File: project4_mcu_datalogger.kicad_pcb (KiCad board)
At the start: 2 copper layers, 49.6 x 30.5 mm, 30 parts, among them J1 Conn_01x09_Pin, J2 Conn_01x04_Pin, J3 Conn_01x04_Pin, J4 Conn_02x03_Odd_Even, U1 24LC1025, U2 DS1337S_T_R, U3 24LC1025, U4 ATMEGA328P-AU, Y1 32.768 KHz, Y2 16 MHz

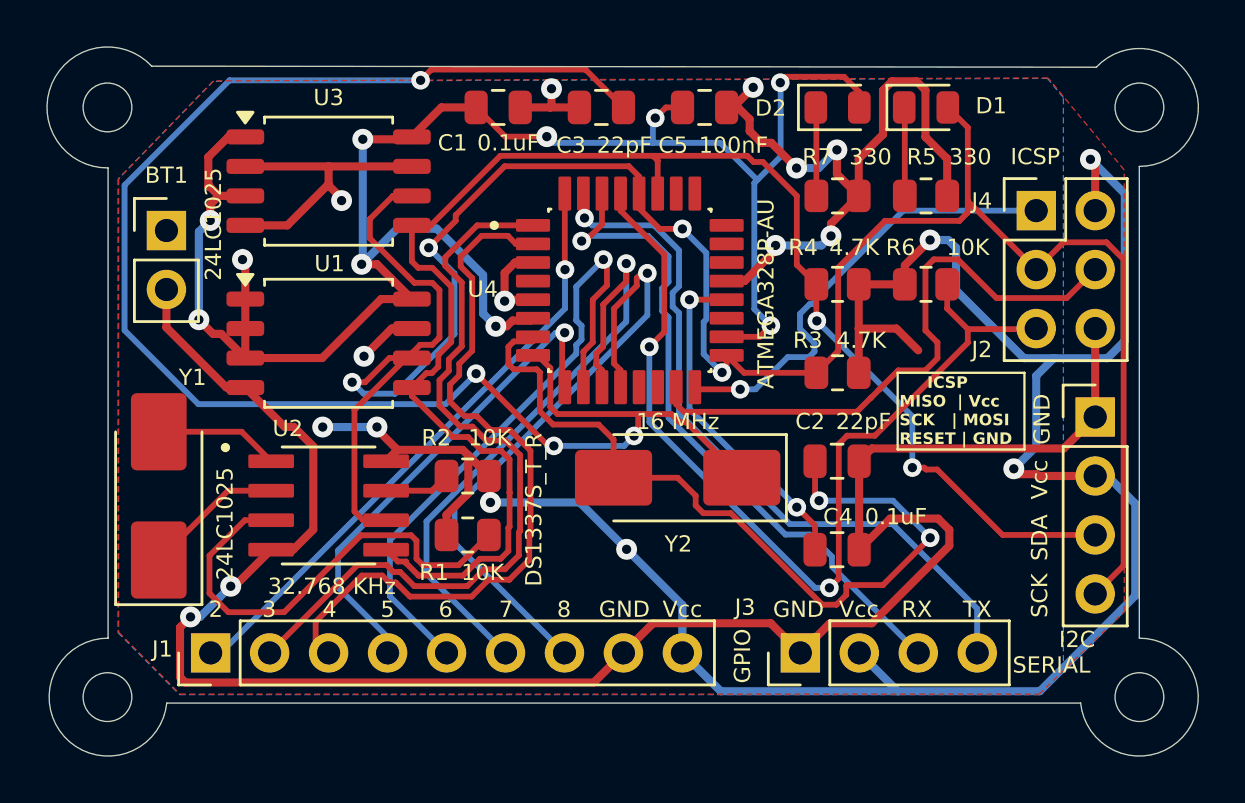
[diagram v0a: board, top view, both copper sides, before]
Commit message: Completed 4-layer pcb routing
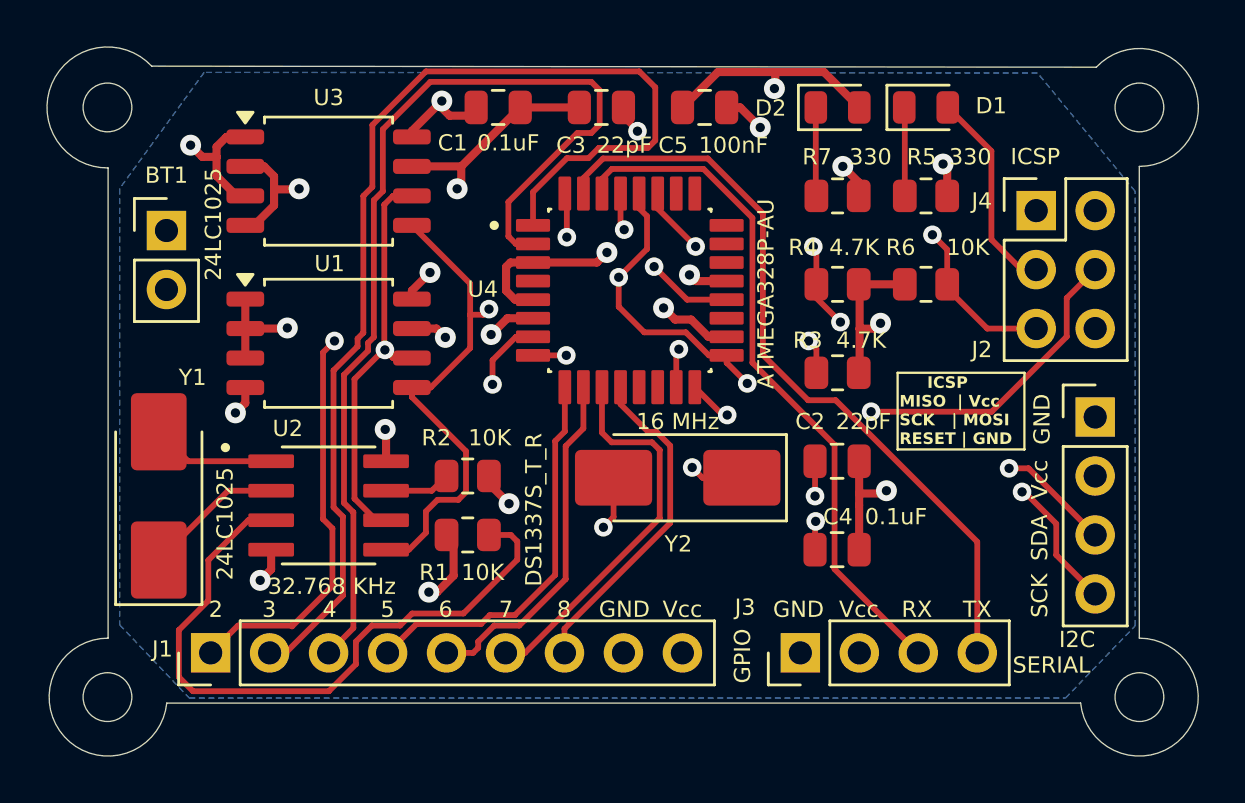
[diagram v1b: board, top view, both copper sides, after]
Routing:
- net /Vcc: track 184.0 -> 58.0 mm, vias 17 -> 11
- net GND: track 138.7 -> 37.5 mm
- net Net-(U4-PB7): track 68.9 -> 23.4 mm, vias 4 -> 3
- net /RESET: track 41.2 -> 22.5 mm
- net /SCK: track 99.3 -> 83.4 mm, vias 4 -> 5
- net /D3: track 33.4 -> 48.6 mm
- net /D8: track 27.5 -> 14.4 mm, vias 1 -> 0
- net /D6: track 27.9 -> 15.2 mm, vias 1 -> 0
- net /D7: track 27.7 -> 16.7 mm, vias 1 -> 0
- net /D4: track 32.8 -> 43.7 mm
- net Net-(U4-PB6): track 35.7 -> 25.2 mm, vias 2 -> 3
- net Net-(U2-~{INTA}): track 20.2 -> 28.9 mm
- net /SDA: track 67.9 -> 60.1 mm, vias 2 -> 5
- net Net-(U4-AREF): track 14.8 -> 21.3 mm
- net /D2: track 26.4 -> 31.2 mm, vias 1 -> 2
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- added copper zone on In2.Cu, net /Vcc
- removed copper zone on F.Cu, net /Vcc
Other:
- copper layers 2 -> 4
